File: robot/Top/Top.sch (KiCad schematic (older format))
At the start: 26 parts, among them J1 Conn_01x02_Male, SW1 SW_DPDT_x2, U2 MCP73831-2-OT, U3 SSD1306

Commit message: Small changes, connectors
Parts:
- added H11, H9: GND, Custom:Mounting_Pad_Power, symbol Custom:MountingPad
- H1: value BAT_MON -> BTMN
- H2: value VBAT_SWITCH -> VSW
- H3: value OLED_~RES -> ORES
- H4: value OLED_SCL -> OSCL
- H5: value OLED_SDA -> OSDA
- H6: value VBUS -> VBS
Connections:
- net GND: now also H11.1 (Pin), H9.1 (Pin)
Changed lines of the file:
@@
 P 5150 2600
 F 0 "H1" H 5050 2550 50  0000 R CNN
-F 1 "BAT_MON" H 5050 2650 50  0000 R CNN
+F 1 "BTMN" H 5050 2650 50  0000 R CNN
 F 2 "Custom:Mounting_Pad_Signal" H 5150 2750 50  0001 C CNN
 F 3 "" H 5150 2750 50  0001 C CNN
@@
 P 7250 4400
 F 0 "H3" H 7400 4350 50  0000 R CNN
-F 1 "OLED_~RES" H 7700 4450 50  0000 R CNN
+F 1 "ORES" H 7500 4450 50  0000 R CNN
 F 2 "Custom:Mounting_Pad_Signal" H 7250 4550 50  0001 C CNN
 F 3 "" H 7250 4550 50  0001 C CNN
@@
 P 7400 4650
 F 0 "H4" H 7550 4600 50  0000 R CNN
-F 1 "OLED_SCL" H 7850 4700 50  0000 R CNN
+F 1 "OSCL" H 7650 4700 50  0000 R CNN
 F 2 "Custom:Mounting_Pad_Signal" H 7400 4800 50  0001 C CNN
 F 3 "" H 7400 4800 50  0001 C CNN
@@
 P 7550 4900
 F 0 "H5" H 7700 4850 50  0000 R CNN
-F 1 "OLED_SDA" H 8000 4950 50  0000 R CNN
+F 1 "OSDA" H 7800 4950 50  0000 R CNN
 F 2 "Custom:Mounting_Pad_Signal" H 7550 5050 50  0001 C CNN
 F 3 "" H 7550 5050 50  0001 C CNN
@@
 P 1800 3100
 F 0 "H2" H 1700 3050 50  0000 R CNN
-F 1 "VBAT_SWITCH" H 1700 3150 50  0000 R CNN
+F 1 "VSW" H 1700 3150 50  0000 R CNN
 F 2 "Custom:Mounting_Pad_Power" H 1800 3250 50  0001 C CNN
 F 3 "" H 1800 3250 50  0001 C CNN
@@
 P 3850 5200
 F 0 "H6" H 3750 5150 50  0000 R CNN
-F 1 "VBUS" H 3750 5250 50  0000 R CNN
+F 1 "VBS" H 3750 5250 50  0000 R CNN
 F 2 "Custom:Mounting_Pad_Power" H 3850 5350 50  0001 C CNN
 F 3 "" H 3850 5350 50  0001 C CNN
@@
 Wire Wire Line
 	3100 6300 3100 6400
+$Comp
+L Custom:MountingPad H9
+U 1 1 5D9B748A
+P 2800 6850
+F 0 "H9" H 2750 6900 50  0000 R CNN
+F 1 "GND" H 2750 6800 50  0000 R CNN
+F 2 "Custom:Mounting_Pad_Power" H 2800 7000 50  0001 C CNN
+F 3 "" H 2800 7000 50  0001 C CNN
+	1    2800 6850
+	1    0    0    -1
+$EndComp
+$Comp
+L power:GND #PWR0103
+U 1 1 5D9B7494
+P 2800 7250
+F 0 "#PWR0103" H 2800 7000 50  0001 C CNN
+F 1 "GND" H 2805 7077 50  0000 C CNN
+F 2 "" H 2800 7250 50  0001 C CNN
+F 3 "" H 2800 7250 50  0001 C CNN
+	1    2800 7250
+	1    0    0    -1
+$EndComp
+Wire Wire Line
+	2800 7150 2800 7250
+$Comp
+L Custom:MountingPad H11
+U 1 1 5D9B749F
+P 3100 6850
+F 0 "H11" H 3050 6900 50  0000 R CNN
+F 1 "GND" H 3050 6800 50  0000 R CNN
+F 2 "Custom:Mounting_Pad_Power" H 3100 7000 50  0001 C CNN
+F 3 "" H 3100 7000 50  0001 C CNN
+	1    3100 6850
+	1    0    0    -1
+$EndComp
+$Comp
+L power:GND #PWR0104
+U 1 1 5D9B74A9
+P 3100 7250
+F 0 "#PWR0104" H 3100 7000 50  0001 C CNN
+F 1 "GND" H 3105 7077 50  0000 C CNN
+F 2 "" H 3100 7250 50  0001 C CNN
+F 3 "" H 3100 7250 50  0001 C CNN
+	1    3100 7250
+	1    0    0    -1
+$EndComp
+Wire Wire Line
+	3100 7150 3100 7250
 $EndSCHEMATC

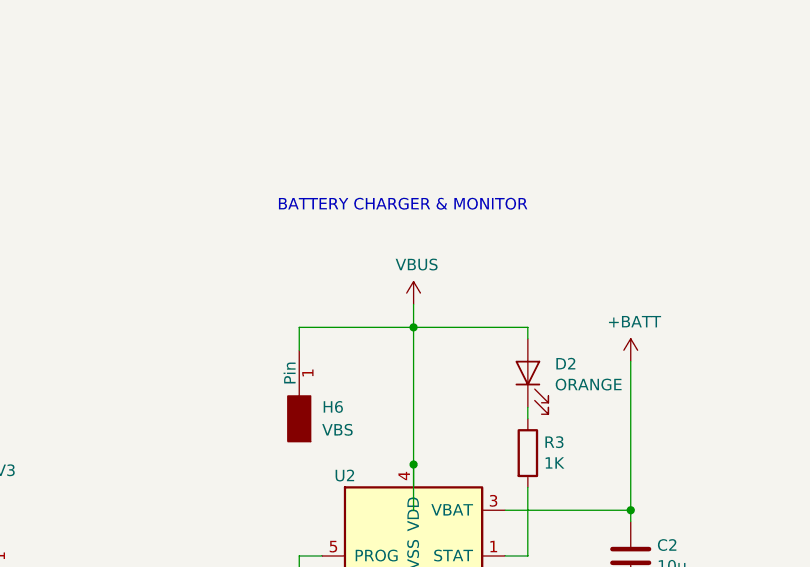
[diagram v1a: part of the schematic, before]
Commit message: Add VBS, Add Silk deco, small changes
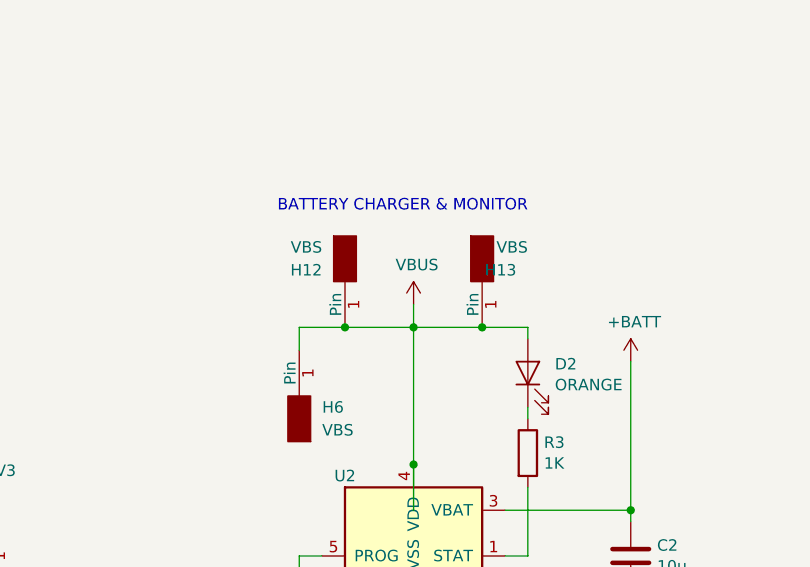
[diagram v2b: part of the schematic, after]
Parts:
- added H12, H13: VBS, Custom:Mounting_Pad_Power, symbol Custom:MountingPad
- D1: footprint Diodes_SMD:D_SOD-123 -> Diode_SMD:D_SOD-123
- D2: footprint LEDs:LED_0603 -> LED_SMD:LED_0603_1608Metric
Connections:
- net VBUS: now also H12.1 (Pin), H13.1 (Pin)
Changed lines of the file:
@@
 F 0 "D2" V 4889 4882 50  0000 R CNN
 F 1 "ORANGE" V 4798 4882 50  0000 R CNN
-F 2 "LEDs:LED_0603" H 4850 5000 50  0001 C CNN
+F 2 "LED_SMD:LED_0603_1608Metric" H 4850 5000 50  0001 C CNN
 F 3 "~" H 4850 5000 50  0001 C CNN
 	1    4850 5000
@@
 F 0 "D1" V 1846 2371 50  0000 R CNN
 F 1 "D_Schottky" V 1755 2371 50  0000 R CNN
-F 2 "Diodes_SMD:D_SOD-123" H 1800 2450 50  0001 C CNN
+F 2 "Diode_SMD:D_SOD-123" H 1800 2450 50  0001 C CNN
 F 3 "~" H 1800 2450 50  0001 C CNN
 	1    1800 2450
@@
 	1800 2750 1800 2800
 Connection ~ 1800 2750
+Wire Wire Line
+	4350 4800 4050 4800
+Wire Wire Line
+	3850 4800 3850 4900
+$Comp
+L Custom:MountingPad H7
+U 1 1 5D7C1B62
+P 2500 6000
+F 0 "H7" H 2650 5950 50  0000 R CNN
+F 1 "3V3" H 2700 6050 50  0000 R CNN
+F 2 "Custom:Mounting_Pad_Power" H 2500 6150 50  0001 C CNN
+F 3 "" H 2500 6150 50  0001 C CNN
+	1    2500 6000
+	-1   0    0    1
+$EndComp
+$Comp
+L power:+3V3 #PWR05
+U 1 1 5D7C22BE
+P 2500 5600
+F 0 "#PWR05" H 2500 5450 50  0001 C CNN
+F 1 "+3V3" H 2515 5773 50  0000 C CNN
+F 2 "" H 2500 5600 50  0001 C CNN
+F 3 "" H 2500 5600 50  0001 C CNN
+	1    2500 5600
+	1    0    0    -1
+$EndComp
+$Comp
+L Custom:MountingPad H8
+U 1 1 5D7C32E1
+P 2800 6000
+F 0 "H8" H 2750 6050 50  0000 R CNN
+F 1 "GND" H 2750 5950 50  0000 R CNN
+F 2 "Custom:Mounting_Pad_Power" H 2800 6150 50  0001 C CNN
+F 3 "" H 2800 6150 50  0001 C CNN
+	1    2800 6000
+	1    0    0    -1
+$EndComp
+$Comp
+L power:GND #PWR010
+U 1 1 5D7C353D
+P 2800 6400
+F 0 "#PWR010" H 2800 6150 50  0001 C CNN
+F 1 "GND" H 2805 6227 50  0000 C CNN
+F 2 "" H 2800 6400 50  0001 C CNN
+F 3 "" H 2800 6400 50  0001 C CNN
+	1    2800 6400
+	1    0    0    -1
+$EndComp
+Wire Wire Line
+	2500 5600 2500 5700
+Wire Wire Line
+	2800 6300 2800 6400
+Wire Wire Line
+	4750 5800 4850 5800
+Wire Wire Line
+	4850 5800 4850 5500
+Wire Wire Line
+	4350 4800 4650 4800
+Wire Wire Line
+	4850 4800 4850 4850
+Connection ~ 4350 5400
+Wire Wire Line
+	4350 5600 4350 5400
+$Comp
+L power:VBUS #PWR0101
+U 1 1 5D8509D5
+P 1150 5550
+F 0 "#PWR0101" H 1150 5400 50  0001 C CNN
+F 1 "VBUS" H 1165 5723 50  0000 C CNN
+F 2 "" H 1150 5550 50  0001 C CNN
+F 3 "" H 1150 5550 50  0001 C CNN
+	1    1150 5550
+	1    0    0    -1
+$EndComp
+$Comp
+L power:PWR_FLAG #FLG0101
+U 1 1 5D850FC1
+P 1150 5650
+F 0 "#FLG0101" H 1150 5725 50  0001 C CNN
+F 1 "PWR_FLAG" H 1150 5823 50  0000 C CNN
+F 2 "" H 1150 5650 50  0001 C CNN
+F 3 "~" H 1150 5650 50  0001 C CNN
+	1    1150 5650
+	-1   0    0    1
+$EndComp
+Wire Wire Line
+	1150 5550 1150 5650
+$Comp
+L Custom:MountingPad H10
+U 1 1 5D7C3320
+P 3100 6000
+F 0 "H10" H 3050 6050 50  0000 R CNN
+F 1 "GND" H 3050 5950 50  0000 R CNN
+F 2 "Custom:Mounting_Pad_Power" H 3100 6150 50  0001 C CNN
+F 3 "" H 3100 6150 50  0001 C CNN
+	1    3100 6000
+	1    0    0    -1
+$EndComp
+$Comp
+L power:GND #PWR0102
+U 1 1 5D7C332A
+P 3100 6400
+F 0 "#PWR0102" H 3100 6150 50  0001 C CNN
+F 1 "GND" H 3105 6227 50  0000 C CNN
+F 2 "" H 3100 6400 50  0001 C CNN
+F 3 "" H 3100 6400 50  0001 C CNN
+	1    3100 6400
+	1    0    0    -1
+$EndComp
+Wire Wire Line
+	3100 6300 3100 6400
+$Comp
+L Custom:MountingPad H9
+U 1 1 5D9B748A
+P 2800 6850
+F 0 "H9" H 2750 6900 50  0000 R CNN
+F 1 "GND" H 2750 6800 50  0000 R CNN
+F 2 "Custom:Mounting_Pad_Power" H 2800 7000 50  0001 C CNN
+F 3 "" H 2800 7000 50  0001 C CNN
+	1    2800 6850
+	1    0    0    -1
+$EndComp
+$Comp
+L power:GND #PWR0103
+U 1 1 5D9B7494
+P 2800 7250
+F 0 "#PWR0103" H 2800 7000 50  0001 C CNN
+F 1 "GND" H 2805 7077 50  0000 C CNN
+F 2 "" H 2800 7250 50  0001 C CNN
+F 3 "" H 2800 7250 50  0001 C CNN
+	1    2800 7250
+	1    0    0    -1
+$EndComp
+Wire Wire Line
+	2800 7150 2800 7250
+$Comp
+L Custom:MountingPad H11
+U 1 1 5D9B749F
+P 3100 6850
+F 0 "H11" H 3050 6900 50  0000 R CNN
+F 1 "GND" H 3050 6800 50  0000 R CNN
+F 2 "Custom:Mounting_Pad_Power" H 3100 7000 50  0001 C CNN
+F 3 "" H 3100 7000 50  0001 C CNN
+	1    3100 6850
+	1    0    0    -1
+$EndComp
+$Comp
+L power:GND #PWR0104
+U 1 1 5D9B74A9
+P 3100 7250
+F 0 "#PWR0104" H 3100 7000 50  0001 C CNN
+F 1 "GND" H 3105 7077 50  0000 C CNN
+F 2 "" H 3100 7250 50  0001 C CNN
+F 3 "" H 3100 7250 50  0001 C CNN
+	1    3100 7250
+	1    0    0    -1
+$EndComp
+Wire Wire Line
+	3100 7150 3100 7250
 $Comp
 L Custom:MountingPad H6
@@
 	-1   0    0    1
 $EndComp
-Wire Wire Line
-	4350 4800 3850 4800
-Wire Wire Line
-	3850 4800 3850 4900
-$Comp
-L Custom:MountingPad H7
-U 1 1 5D7C1B62
-P 2500 6000
-F 0 "H7" H 2650 5950 50  0000 R CNN
-F 1 "3V3" H 2700 6050 50  0000 R CNN
-F 2 "Custom:Mounting_Pad_Power" H 2500 6150 50  0001 C CNN
-F 3 "" H 2500 6150 50  0001 C CNN
-	1    2500 6000
-	-1   0    0    1
-$EndComp
-$Comp
-L power:+3V3 #PWR05
-U 1 1 5D7C22BE
-P 2500 5600
-F 0 "#PWR05" H 2500 5450 50  0001 C CNN
-F 1 "+3V3" H 2515 5773 50  0000 C CNN
-F 2 "" H 2500 5600 50  0001 C CNN
-F 3 "" H 2500 5600 50  0001 C CNN
-	1    2500 5600
-	1    0    0    -1
-$EndComp
-$Comp
-L Custom:MountingPad H8
-U 1 1 5D7C32E1
-P 2800 6000
-F 0 "H8" H 2750 6050 50  0000 R CNN
-F 1 "GND" H 2750 5950 50  0000 R CNN
-F 2 "Custom:Mounting_Pad_Power" H 2800 6150 50  0001 C CNN
-F 3 "" H 2800 6150 50  0001 C CNN
-	1    2800 6000
-	1    0    0    -1
-$EndComp
-$Comp
-L power:GND #PWR010
-U 1 1 5D7C353D
-P 2800 6400
-F 0 "#PWR010" H 2800 6150 50  0001 C CNN
-F 1 "GND" H 2805 6227 50  0000 C CNN
-F 2 "" H 2800 6400 50  0001 C CNN
-F 3 "" H 2800 6400 50  0001 C CNN
-	1    2800 6400
-	1    0    0    -1
-$EndComp
-Wire Wire Line
-	2500 5600 2500 5700
-Wire Wire Line
-	2800 6300 2800 6400
-Wire Wire Line
-	4750 5800 4850 5800
-Wire Wire Line
-	4850 5800 4850 5500
-Wire Wire Line
-	4350 4800 4850 4800
-Wire Wire Line
-	4850 4800 4850 4850
-Connection ~ 4350 5400
-Wire Wire Line
-	4350 5600 4350 5400
-$Comp
-L power:VBUS #PWR0101
-U 1 1 5D8509D5
-P 1150 5550
-F 0 "#PWR0101" H 1150 5400 50  0001 C CNN
-F 1 "VBUS" H 1165 5723 50  0000 C CNN
-F 2 "" H 1150 5550 50  0001 C CNN
-F 3 "" H 1150 5550 50  0001 C CNN
-	1    1150 5550
-	1    0    0    -1
-$EndComp
-$Comp
-L power:PWR_FLAG #FLG0101
-U 1 1 5D850FC1
-P 1150 5650
-F 0 "#FLG0101" H 1150 5725 50  0001 C CNN
-F 1 "PWR_FLAG" H 1150 5823 50  0000 C CNN
-F 2 "" H 1150 5650 50  0001 C CNN
-F 3 "~" H 1150 5650 50  0001 C CNN
-	1    1150 5650
-	-1   0    0    1
-$EndComp
-Wire Wire Line
-	1150 5550 1150 5650
-$Comp
-L Custom:MountingPad H10
-U 1 1 5D7C3320
-P 3100 6000
-F 0 "H10" H 3050 6050 50  0000 R CNN
-F 1 "GND" H 3050 5950 50  0000 R CNN
-F 2 "Custom:Mounting_Pad_Power" H 3100 6150 50  0001 C CNN
-F 3 "" H 3100 6150 50  0001 C CNN
-	1    3100 6000
-	1    0    0    -1
-$EndComp
-$Comp
-L power:GND #PWR0102
-U 1 1 5D7C332A
-P 3100 6400
-F 0 "#PWR0102" H 3100 6150 50  0001 C CNN
-F 1 "GND" H 3105 6227 50  0000 C CNN
-F 2 "" H 3100 6400 50  0001 C CNN
-F 3 "" H 3100 6400 50  0001 C CNN
-	1    3100 6400
-	1    0    0    -1
-$EndComp
-Wire Wire Line
-	3100 6300 3100 6400
-$Comp
-L Custom:MountingPad H9
-U 1 1 5D9B748A
-P 2800 6850
-F 0 "H9" H 2750 6900 50  0000 R CNN
-F 1 "GND" H 2750 6800 50  0000 R CNN
-F 2 "Custom:Mounting_Pad_Power" H 2800 7000 50  0001 C CNN
-F 3 "" H 2800 7000 50  0001 C CNN
-	1    2800 6850
-	1    0    0    -1
-$EndComp
-$Comp
-L power:GND #PWR0103
-U 1 1 5D9B7494
-P 2800 7250
-F 0 "#PWR0103" H 2800 7000 50  0001 C CNN
-F 1 "GND" H 2805 7077 50  0000 C CNN
-F 2 "" H 2800 7250 50  0001 C CNN
-F 3 "" H 2800 7250 50  0001 C CNN
-	1    2800 7250
-	1    0    0    -1
-$EndComp
-Wire Wire Line
-	2800 7150 2800 7250
-$Comp
-L Custom:MountingPad H11
-U 1 1 5D9B749F
-P 3100 6850
-F 0 "H11" H 3050 6900 50  0000 R CNN
-F 1 "GND" H 3050 6800 50  0000 R CNN
-F 2 "Custom:Mounting_Pad_Power" H 3100 7000 50  0001 C CNN
-F 3 "" H 3100 7000 50  0001 C CNN
-	1    3100 6850
-	1    0    0    -1
-$EndComp
-$Comp
-L power:GND #PWR0104
-U 1 1 5D9B74A9
-P 3100 7250
-F 0 "#PWR0104" H 3100 7000 50  0001 C CNN
-F 1 "GND" H 3105 7077 50  0000 C CNN
-F 2 "" H 3100 7250 50  0001 C CNN
-F 3 "" H 3100 7250 50  0001 C CNN
-	1    3100 7250
-	1    0    0    -1
-$EndComp
-Wire Wire Line
-	3100 7150 3100 7250
+$Comp
+L Custom:MountingPad H12
+U 1 1 5D9A66BC
+P 4050 4500
+F 0 "H12" H 3950 4450 50  0000 R CNN
+F 1 "VBS" H 3950 4550 50  0000 R CNN
+F 2 "Custom:Mounting_Pad_Power" H 4050 4650 50  0001 C CNN
+F 3 "" H 4050 4650 50  0001 C CNN
+	1    4050 4500
+	1    0    0    -1
+$EndComp
+Connection ~ 4050 4800
+Wire Wire Line
+	4050 4800 3850 4800
+$Comp
+L Custom:MountingPad H13
+U 1 1 5D9A6DFE
+P 4650 4500
+F 0 "H13" H 4800 4450 50  0000 R CNN
+F 1 "VBS" H 4850 4550 50  0000 R CNN
+F 2 "Custom:Mounting_Pad_Power" H 4650 4650 50  0001 C CNN
+F 3 "" H 4650 4650 50  0001 C CNN
+	1    4650 4500
+	1    0    0    -1
+$EndComp
+Connection ~ 4650 4800
+Wire Wire Line
+	4650 4800 4850 4800
 $EndSCHEMATC

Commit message: BOM items
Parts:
- C2: value 10µ -> 22µ; LCSC (none) -> C5674; Manufacturer Nbr (none) -> CL21A226MQQNNNE
- C3, C4, C5: LCSC (none) -> C106837; Manufacturer Nbr (none) -> CC0805ZRY5V8BB105
- C6, C7: LCSC (none) -> C87998; Manufacturer Nbr (none) -> CL21B475KPFNNNE
- D1: LCSC (none) -> C181204; Manufacturer Nbr (none) -> SD103AW
- D2: LCSC (none) -> C84269; Manufacturer Nbr (none) -> FC-DA1608HOK-600H
- R1, R2: LCSC (none) -> C25611; Manufacturer Nbr (none) -> 0805W8J0104T5E
- R3: LCSC (none) -> C25623; Manufacturer Nbr (none) -> 0805W8J0102T5E
- R4: value 5K -> 4.7K; LCSC (none) -> C26022; Manufacturer Nbr (none) -> 0805W8J0472T5E
- R5: LCSC (none) -> C17629; Manufacturer Nbr (none) -> 0805W8F3303T5E
- SW1: Farnell (none) -> 2320017; LCSC (none) -> C221660; Manufacturer Nbr (none) -> JS102011SAQN
- U2: LCSC (none) -> C14879; Manufacturer Nbr (none) -> MCP73831T-2ATI/OT
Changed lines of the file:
@@
 F 2 "Package_TO_SOT_SMD:SOT-23-5" H 4400 5450 50  0001 L CIN
 F 3 "http://ww1.microchip.com/downloads/en/DeviceDoc/20001984g.pdf" H 4200 5650 50  0001 C CNN
+F 4 "C14879" H 4350 5700 50  0001 C CNN "LCSC"
+F 5 "MCP73831T-2ATI/OT" H 4350 5700 50  0001 C CNN "Manufacturer Nbr"
 	1    4350 5700
 	1    0    0    -1
@@
 P 3850 6050
 F 0 "R4" H 3920 6096 50  0000 L CNN
-F 1 "5K" H 3920 6005 50  0000 L CNN
+F 1 "4.7K" H 3920 6005 50  0000 L CNN
 F 2 "Resistor_SMD:R_0805_2012Metric" V 3780 6050 50  0001 C CNN
 F 3 "~" H 3850 6050 50  0001 C CNN
+F 4 "C26022" H 3850 6050 50  0001 C CNN "LCSC"
+F 5 "0805W8J0472T5E" H 3850 6050 50  0001 C CNN "Manufacturer Nbr"
 	1    3850 6050
 	1    0    0    -1
@@
 P 5300 5800
 F 0 "C2" H 5415 5846 50  0000 L CNN
-F 1 "10µ" H 5415 5755 50  0000 L CNN
+F 1 "22µ" H 5415 5755 50  0000 L CNN
 F 2 "Capacitor_SMD:C_0805_2012Metric" H 5338 5650 50  0001 C CNN
 F 3 "~" H 5300 5800 50  0001 C CNN
+F 4 "C5674" H 5300 5800 50  0001 C CNN "LCSC"
+F 5 "CL21A226MQQNNNE" H 5300 5800 50  0001 C CNN "Manufacturer Nbr"
 	1    5300 5800
 	1    0    0    -1
@@
 F 2 "LED_SMD:LED_0603_1608Metric" H 4850 5000 50  0001 C CNN
 F 3 "~" H 4850 5000 50  0001 C CNN
+F 4 "C84269" H 4850 5000 50  0001 C CNN "LCSC"
+F 5 "FC-DA1608HOK-600H" H 4850 5000 50  0001 C CNN "Manufacturer Nbr"
 	1    4850 5000
 	0    -1   -1   0
@@
 F 2 "Resistor_SMD:R_0805_2012Metric" V 4780 5350 50  0001 C CNN
 F 3 "~" H 4850 5350 50  0001 C CNN
+F 4 "C25623" H 4850 5350 50  0001 C CNN "LCSC"
+F 5 "0805W8J0102T5E" H 4850 5350 50  0001 C CNN "Manufacturer Nbr"
 	1    4850 5350
 	1    0    0    -1
@@
 F 2 "Resistor_SMD:R_0805_2012Metric" V 4580 1900 50  0001 C CNN
 F 3 "~" H 4650 1900 50  0001 C CNN
+F 4 "C25611" H 4650 1900 50  0001 C CNN "LCSC"
+F 5 "0805W8J0104T5E" H 4650 1900 50  0001 C CNN "Manufacturer Nbr"
 	1    4650 1900
 	1    0    0    -1
@@
 F 2 "Resistor_SMD:R_0805_2012Metric" V 4580 2400 50  0001 C CNN
 F 3 "~" H 4650 2400 50  0001 C CNN
+F 4 "C25611" H 4650 2400 50  0001 C CNN "LCSC"
+F 5 "0805W8J0104T5E" H 4650 2400 50  0001 C CNN "Manufacturer Nbr"
 	1    4650 2400
 	1    0    0    -1
@@
 F 2 "Diode_SMD:D_SOD-123" H 1800 2450 50  0001 C CNN
 F 3 "~" H 1800 2450 50  0001 C CNN
+F 4 "C181204" H 1800 2450 50  0001 C CNN "LCSC"
+F 5 "SD103AW" H 1800 2450 50  0001 C CNN "Manufacturer Nbr"
 	1    1800 2450
 	0    -1   -1   0
@@
 F 2 "Custom:JS102011SAQN" H 1800 1850 50  0001 C CNN
 F 3 "~" H 1800 1850 50  0001 C CNN
+F 4 "2320017" H 1800 1850 50  0001 C CNN "Farnell"
+F 5 "C221660" H 1800 1850 50  0001 C CNN "LCSC"
+F 6 "JS102011SAQN" H 1800 1850 50  0001 C CNN "Manufacturer Nbr"
 	1    1800 1850
 	0    -1   -1   0
@@
 F 2 "Capacitor_SMD:C_0805_2012Metric" H 8738 2400 50  0001 C CNN
 F 3 "~" H 8700 2550 50  0001 C CNN
+F 4 "C106837" H 8700 2550 50  0001 C CNN "LCSC"
+F 5 "CC0805ZRY5V8BB105" H 8700 2550 50  0001 C CNN "Manufacturer Nbr"
 	1    8700 2550
 	0    1    1    0
@@
 F 2 "Capacitor_SMD:C_0805_2012Metric" H 8738 2700 50  0001 C CNN
 F 3 "~" H 8700 2850 50  0001 C CNN
+F 4 "C106837" H 8700 2850 50  0001 C CNN "LCSC"
+F 5 "CC0805ZRY5V8BB105" H 8700 2850 50  0001 C CNN "Manufacturer Nbr"
 	1    8700 2850
 	0    1    1    0
@@
 F 2 "Capacitor_SMD:C_0805_2012Metric" H 8738 3000 50  0001 C CNN
 F 3 "~" H 8700 3150 50  0001 C CNN
+F 4 "C106837" H 8700 3150 50  0001 C CNN "LCSC"
+F 5 "CC0805ZRY5V8BB105" H 8700 3150 50  0001 C CNN "Manufacturer Nbr"
 	1    8700 3150
 	0    1    1    0
@@
 F 2 "Capacitor_SMD:C_0805_2012Metric" H 8738 4200 50  0001 C CNN
 F 3 "~" H 8700 4350 50  0001 C CNN
+F 4 "C87998" H 8700 4350 50  0001 C CNN "LCSC"
+F 5 "CL21B475KPFNNNE" H 8700 4350 50  0001 C CNN "Manufacturer Nbr"
 	1    8700 4350
 	0    1    1    0
@@
 F 2 "Capacitor_SMD:C_0805_2012Metric" H 8738 4450 50  0001 C CNN
 F 3 "~" H 8700 4600 50  0001 C CNN
+F 4 "C87998" H 8700 4600 50  0001 C CNN "LCSC"
+F 5 "CL21B475KPFNNNE" H 8700 4600 50  0001 C CNN "Manufacturer Nbr"
 	1    8700 4600
 	0    -1   -1   0
@@
 F 2 "Resistor_SMD:R_0805_2012Metric" V 8630 4150 50  0001 C CNN
 F 3 "~" H 8700 4150 50  0001 C CNN
+F 4 "C17629" H 8700 4150 50  0001 C CNN "LCSC"
+F 5 "0805W8F3303T5E" H 8700 4150 50  0001 C CNN "Manufacturer Nbr"
 	1    8700 4150
 	0    -1   -1   0
